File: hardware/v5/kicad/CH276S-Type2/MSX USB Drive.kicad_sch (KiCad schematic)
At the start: 11 parts, among them J1 AVR-JTAG-10, J2 Conn_02x08_Odd_Even, SW1 SK12D07VG4, U2 EPM7064STC44-7, U3 M29F400M

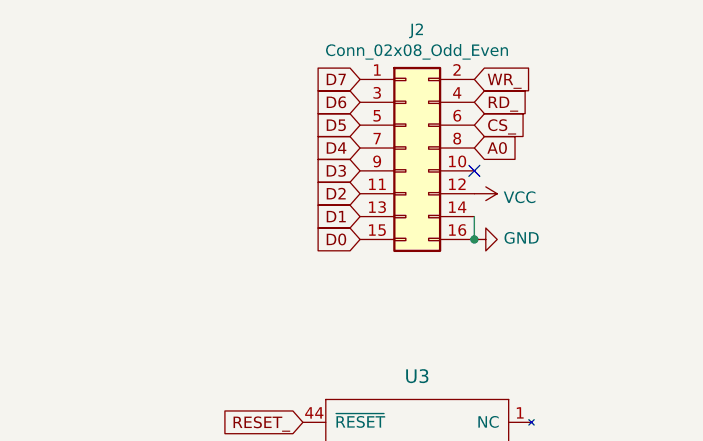
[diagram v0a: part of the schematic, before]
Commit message: cpld code and adjustments for v5
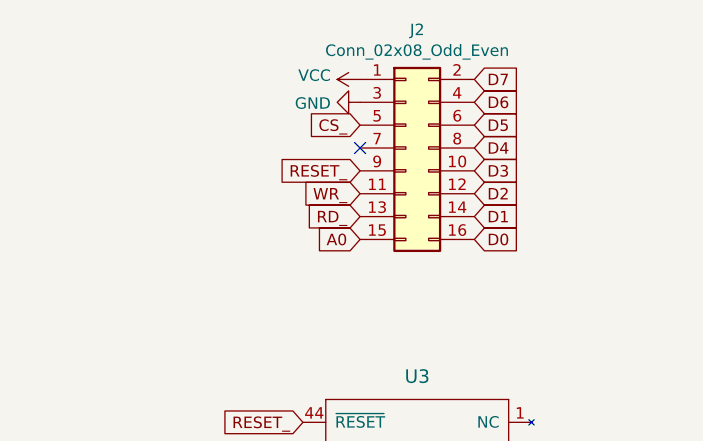
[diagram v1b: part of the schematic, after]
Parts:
- SW1: footprint SK12D07VG4 -> libraries:SK12D07VG4
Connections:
- net A0: now also J2.15 (Pin_15); no longer J2.8 (Pin_8)
- net CS_: now also J2.5 (Pin_5); no longer J2.6 (Pin_6)
- net D0: now also J2.16 (Pin_16); no longer J2.15 (Pin_15)
- net D1: now also J2.14 (Pin_14); no longer J2.13 (Pin_13)
- net D2: now also J2.12 (Pin_12); no longer J2.11 (Pin_11)
- net D3: now also J2.10 (Pin_10); no longer J2.9 (Pin_9)
- net D4: now also J2.8 (Pin_8); no longer J2.7 (Pin_7)
- net D5: now also J2.6 (Pin_6); no longer J2.5 (Pin_5)
- net D6: now also J2.4 (Pin_4); no longer J2.3 (Pin_3)
- net D7: now also J2.2 (Pin_2); no longer J2.1 (Pin_1)
- net GND: now also J2.3 (Pin_3); no longer J2.14 (Pin_14), J2.16 (Pin_16)
- net RD_: now also J2.13 (Pin_13); no longer J2.4 (Pin_4)
- net RESET_: now also J2.9 (Pin_9)
- net VCC: now also J2.1 (Pin_1); no longer J2.12 (Pin_12)
- net WR_: now also J2.11 (Pin_11); no longer J2.2 (Pin_2)
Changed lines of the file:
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@@
 	(title_block
 		(title "MSX-USB")
-		(date "2024-10-12")
+		(date "2024-11-18")
 		(rev "5.0")
 		(company "The Retro Hacker")
+		(comment 1 "Suitable for the CH376S Type 2")
 		(comment 2 "New PCB version, CPLD code by The Retro Hacker")
 		(comment 3 "Original project by S0urceror")
@@
 	)
 	(junction
-		(at 238.76 43.18)
-		(diameter 0)
-		(color 0 0 0 0)
-	)
-	(junction
 		(at 111.76 82.55)
 		(diameter 0)
@@
 	)
 	(no_connect
-		(at 238.76 35.56)
-	)
-	(no_connect
 		(at 245.11 91.44)
 	)
@@
 	)
 	(no_connect
+		(at 226.06 33.02)
+	)
+	(no_connect
 		(at 245.11 93.98)
 	)
@@
 	(wire
 		(pts
-			(xy 238.76 40.64) (xy 238.76 43.18)
-		)
-		(stroke
-			(width 0)
-			(type default)
-		)
-	)
-	(wire
-		(pts
 			(xy 260.35 133.35) (xy 259.08 133.35)
 		)
@@
 	(global_label "RD_"
 		(shape input)
-		(at 238.76 27.94 0)
+		(at 226.06 40.64 180)
 		(fields_autoplaced yes)
 		(effects
@@
 				(size 1.27 1.27)
 			)
-			(justify left)
+			(justify right)
 		)
 		(property "Intersheetrefs" "${INTERSHEET_REFS}"
-			(at 244.5986 27.94 0)
+			(at 220.2214 40.64 0)
 			(effects
 				(font
 					(size 1.27 1.27)
 				)
-				(justify left)
+				(justify right)
 				(hide yes)
 			)
@@
 	(global_label "A0"
 		(shape input)
-		(at 238.76 33.02 0)
+		(at 226.06 43.18 180)
 		(fields_autoplaced yes)
 		(effects
@@
 				(size 1.27 1.27)
 			)
-			(justify left)
+			(justify right)
 		)
 		(property "Intersheetrefs" "${INTERSHEET_REFS}"
-			(at 243.3891 33.02 0)
+			(at 221.4309 43.18 0)
 			(effects
 				(font
 					(size 1.27 1.27)
 				)
-				(justify left)
+				(justify right)
 				(hide yes)
 			)
@@
 	(global_label "D3"
 		(shape input)
-		(at 226.06 35.56 180)
+		(at 238.76 35.56 0)
 		(fields_autoplaced yes)
 		(effects
@@
 				(size 1.27 1.27)
 			)
-			(justify right)
+			(justify left)
 		)
 		(property "Intersheetrefs" "${INTERSHEET_REFS}"
-			(at 221.2495 35.56 0)
+			(at 243.5705 35.56 0)
 			(effects
 				(font
 					(size 1.27 1.27)
 				)
-				(justify right)
+				(justify left)
 				(hide yes)
 			)
@@
 	(global_label "D1"
 		(shape input)
-		(at 226.06 40.64 180)
+		(at 238.76 40.64 0)
 		(fields_autoplaced yes)
 		(effects
@@
 				(size 1.27 1.27)
 			)
-			(justify right)
+			(justify left)
 		)
 		(property "Intersheetrefs" "${INTERSHEET_REFS}"
-			(at 221.2495 40.64 0)
+			(at 243.5705 40.64 0)
 			(effects
 				(font
 					(size 1.27 1.27)
 				)
-				(justify right)
+				(justify left)
 				(hide yes)
 			)
@@
 	(global_label "WR_"
 		(shape input)
-		(at 238.76 25.4 0)
+		(at 226.06 38.1 180)
 		(fields_autoplaced yes)
 		(effects
@@
 				(size 1.27 1.27)
 			)
-			(justify left)
+			(justify right)
 		)
 		(property "Intersheetrefs" "${INTERSHEET_REFS}"
-			(at 244.78 25.4 0)
+			(at 220.04 38.1 0)
 			(effects
 				(font
 					(size 1.27 1.27)
 				)
-				(justify left)
+				(justify right)
 				(hide yes)
 			)
@@
 	(global_label "D2"
 		(shape input)
-		(at 226.06 38.1 180)
+		(at 238.76 38.1 0)
 		(fields_autoplaced yes)
 		(effects
@@
 				(size 1.27 1.27)
 			)
-			(justify right)
+			(justify left)
 		)
 		(property "Intersheetrefs" "${INTERSHEET_REFS}"
-			(at 221.2495 38.1 0)
+			(at 243.5705 38.1 0)
 			(effects
 				(font
 					(size 1.27 1.27)
 				)
-				(justify right)
+				(justify left)
 				(hide yes)
 			)
@@
 	(global_label "D5"
 		(shape input)
-		(at 226.06 30.48 180)
+		(at 238.76 30.48 0)
 		(fields_autoplaced yes)
 		(effects
@@
 				(size 1.27 1.27)
 			)
-			(justify right)
+			(justify left)
 		)
 		(property "Intersheetrefs" "${INTERSHEET_REFS}"
-			(at 221.2495 30.48 0)
+			(at 243.5705 30.48 0)
 			(effects
 				(font
 					(size 1.27 1.27)
 				)
-				(justify right)
+				(justify left)
 				(hide yes)
 			)
@@
 	(global_label "D6"
 		(shape input)
-		(at 226.06 27.94 180)
+		(at 238.76 27.94 0)
 		(fields_autoplaced yes)
 		(effects
@@
 				(size 1.27 1.27)
 			)
-			(justify right)
+			(justify left)
 		)
 		(property "Intersheetrefs" "${INTERSHEET_REFS}"
-			(at 221.2495 27.94 0)
+			(at 243.5705 27.94 0)
 			(effects
 				(font
 					(size 1.27 1.27)
 				)
-				(justify right)
+				(justify left)
 				(hide yes)
 			)
@@
 	(global_label "D7"
 		(shape input)
-		(at 226.06 25.4 180)
+		(at 238.76 25.4 0)
 		(fields_autoplaced yes)
 		(effects
@@
 				(size 1.27 1.27)
 			)
-			(justify right)
+			(justify left)
 		)
 		(property "Intersheetrefs" "${INTERSHEET_REFS}"
-			(at 221.2495 25.4 0)
+			(at 243.5705 25.4 0)
 			(effects
 				(font
 					(size 1.27 1.27)
 				)
-				(justify right)
+				(justify left)
 				(hide yes)
 			)
@@
 		)
 	)
+	(global_label "RESET_"
+		(shape input)
+		(at 226.06 35.56 180)
+		(fields_autoplaced yes)
+		(effects
+			(font
+				(size 1.27 1.27)
+			)
+			(justify right)
+		)
+		(property "Intersheetrefs" "${INTERSHEET_REFS}"
+			(at 217.0163 35.56 0)
+			(effects
+				(font
+					(size 1.27 1.27)
+				)
+				(justify right)
+				(hide yes)
+			)
+		)
+	)
 	(global_label "D0"
 		(shape input)
@@
 	(global_label "D4"
 		(shape input)
-		(at 226.06 33.02 180)
+		(at 238.76 33.02 0)
 		(fields_autoplaced yes)
 		(effects
@@
 				(size 1.27 1.27)
 			)
-			(justify right)
+			(justify left)
 		)
 		(property "Intersheetrefs" "${INTERSHEET_REFS}"
-			(at 221.2495 33.02 0)
+			(at 243.5705 33.02 0)
 			(effects
 				(font
 					(size 1.27 1.27)
 				)
-				(justify right)
+				(justify left)
 				(hide yes)
 			)
@@
 	(global_label "CS_"
 		(shape input)
-		(at 238.76 30.48 0)
+		(at 226.06 30.48 180)
 		(fields_autoplaced yes)
 		(effects
@@
 				(size 1.27 1.27)
 			)
-			(justify left)
+			(justify right)
 		)
 		(property "Intersheetrefs" "${INTERSHEET_REFS}"
-			(at 244.5381 30.48 0)
+			(at 220.2819 30.48 0)
 			(effects
 				(font
 					(size 1.27 1.27)
 				)
-				(justify left)
+				(justify right)
 				(hide yes)
 			)
@@
 	(global_label "D0"
 		(shape input)
-		(at 226.06 43.18 180)
+		(at 238.76 43.18 0)
 		(fields_autoplaced yes)
 		(effects
@@
 				(size 1.27 1.27)
 			)
-			(justify right)
+			(justify left)
 		)
 		(property "Intersheetrefs" "${INTERSHEET_REFS}"
-			(at 221.2495 43.18 0)
+			(at 243.5705 43.18 0)
 			(effects
 				(font
 					(size 1.27 1.27)
 				)
-				(justify right)
+				(justify left)
 				(hide yes)
 			)
@@
 	(symbol
 		(lib_id "power:GND")
-		(at 238.76 43.18 90)
+		(at 226.06 27.94 270)
 		(unit 1)
 		(exclude_from_sim no)
@@
 		(dnp no)
 		(property "Reference" "#PWR011"
-			(at 245.11 43.18 0)
+			(at 219.71 27.94 0)
 			(effects
 				(font
@@
 		)
 		(property "Value" "GND"
-			(at 242.0112 43.053 90)
+			(at 222.8088 28.067 90)
 			(effects
 				(font
@@
 		)
 		(property "Footprint" ""
-			(at 238.76 43.18 0)
+			(at 226.06 27.94 0)
 			(effects
 				(font
@@
 		)
 		(property "Datasheet" ""
-			(at 238.76 43.18 0)
+			(at 226.06 27.94 0)
 			(effects
 				(font
@@
 		)
 		(property "Description" ""
-			(at 238.76 43.18 0)
+			(at 226.06 27.94 0)
 			(effects
 				(font
@@
 	(symbol
 		(lib_id "power:VCC")
-		(at 238.76 38.1 270)
+		(at 226.06 25.4 90)
 		(unit 1)
 		(exclude_from_sim no)
@@
 		(dnp no)
 		(property "Reference" "#PWR010"
-			(at 234.95 38.1 0)
+			(at 229.87 25.4 0)
 			(effects
 				(font
@@
 		)
 		(property "Value" "VCC"
-			(at 242.0112 38.5318 90)
+			(at 222.8088 24.9682 90)
 			(effects
 				(font
@@
 		)
 		(property "Footprint" ""
-			(at 238.76 38.1 0)
+			(at 226.06 25.4 0)
 			(effects
 				(font
@@
 		)
 		(property "Datasheet" ""
-			(at 238.76 38.1 0)
+			(at 226.06 25.4 0)
 			(effects
 				(font
@@
 		)
 		(property "Description" ""
-			(at 238.76 38.1 0)
+			(at 226.06 25.4 0)
 			(effects
 				(font
@@
 			)
 		)
-		(property "Footprint" "SK12D07VG4"
+		(property "Footprint" "libraries:SK12D07VG4"
 			(at 106.68 168.91 0)
 			(effects

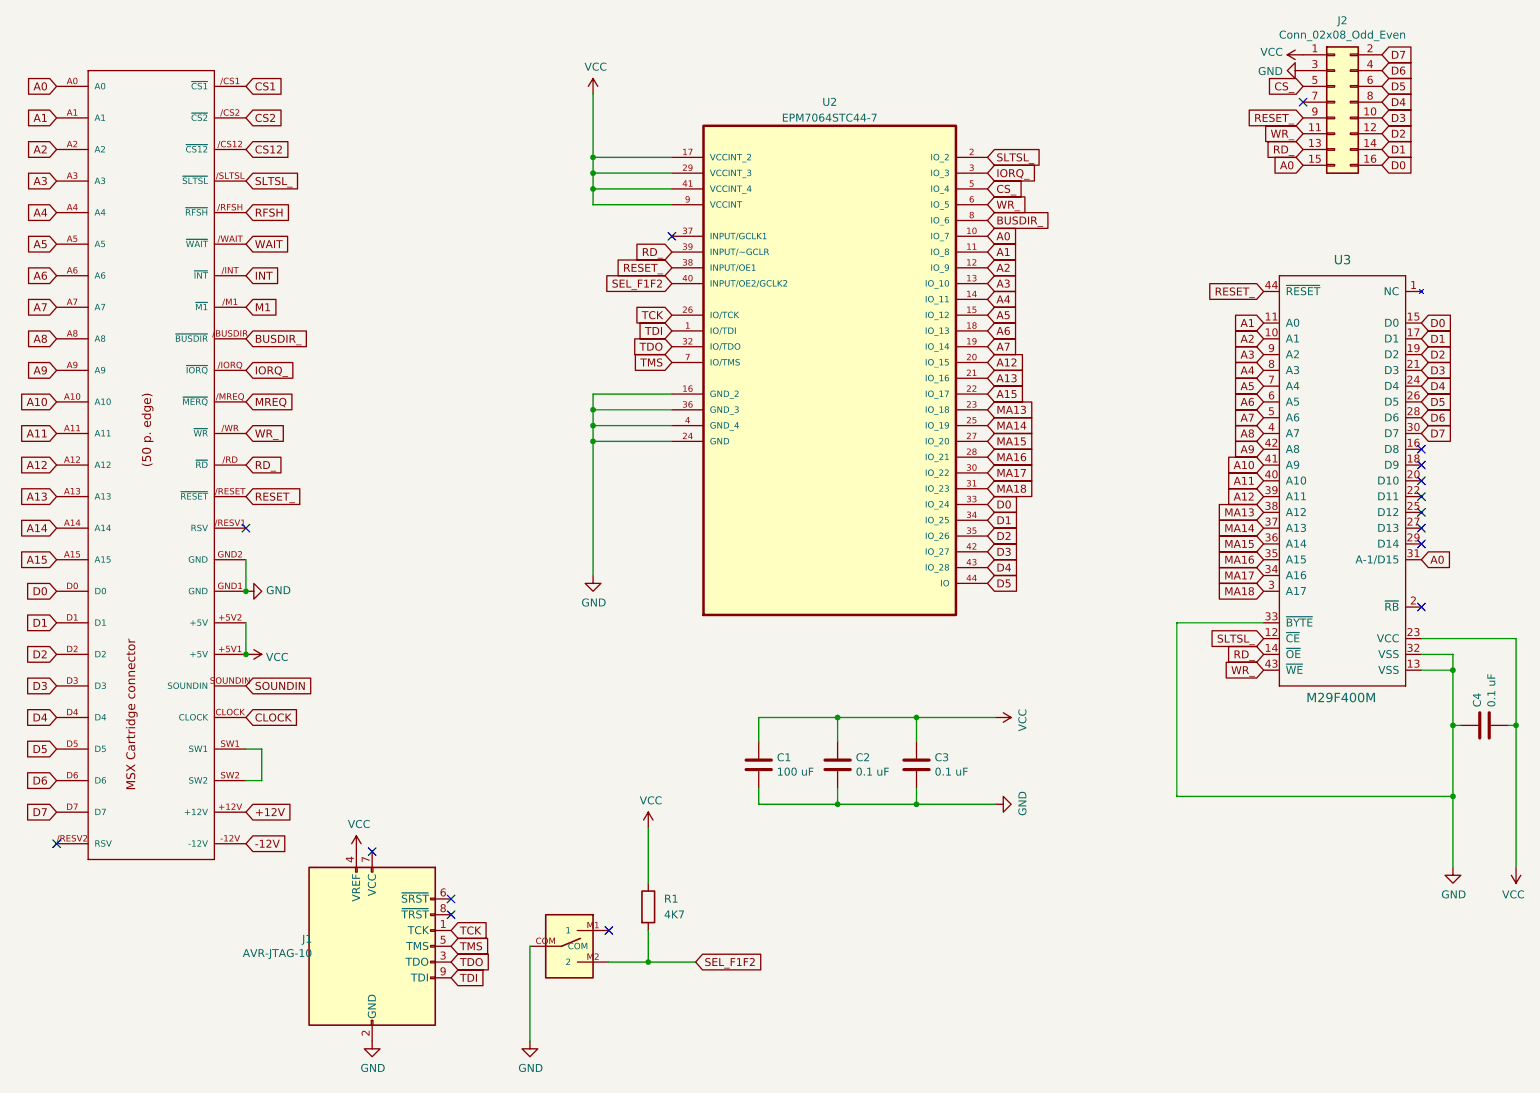
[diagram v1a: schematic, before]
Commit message: PCB adjustments for v5
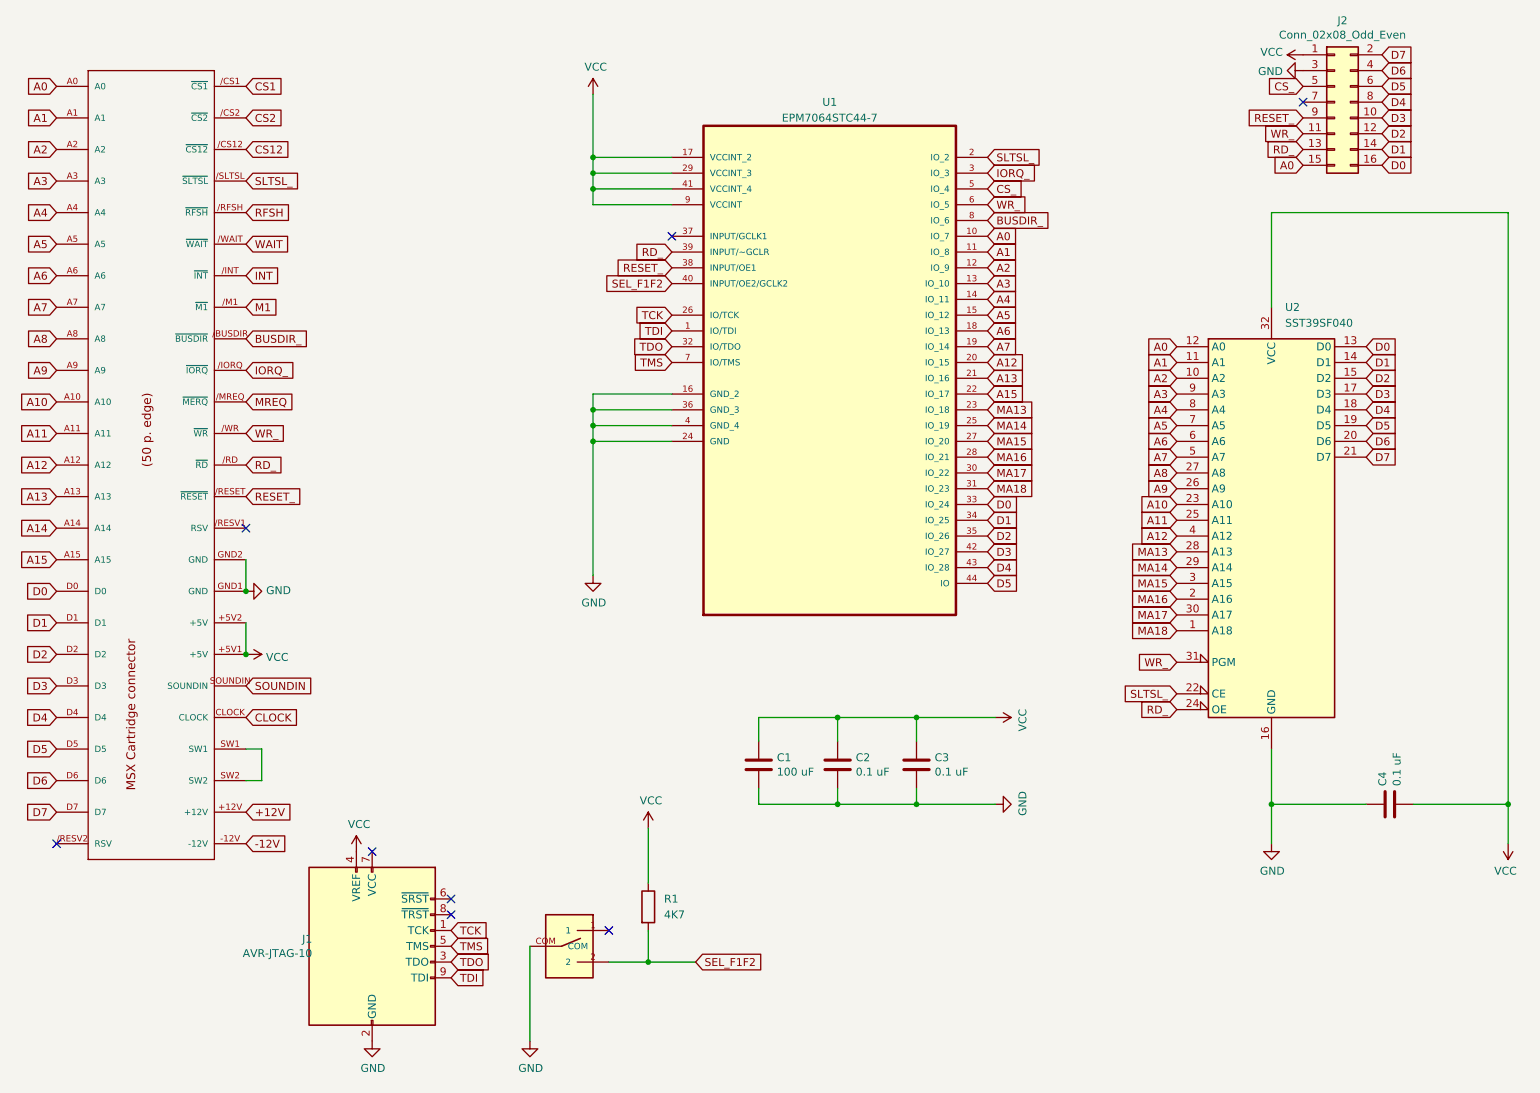
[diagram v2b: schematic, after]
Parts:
- removed U3: M29F400M, libraries:SO44, symbol m29f400m:M29F400M
- added U2: SST39SF040, Package_LCC:PLCC-32_THT-Socket, symbol Memory_Flash:SST39SF040
- SW1: footprint libraries:SK12D07VG4 -> SK12D07VG4
- renumbered U2 to U1
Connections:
- net A0: now also U2.12 (A0)
- net A1: now also U2.11 (A1)
- net A10: now also U2.23 (A10)
- net A11: now also U2.25 (A11)
- net A12: now also U2.4 (A12)
- net A2: now also U2.10 (A2)
- net A3: now also U2.9 (A3)
- net A4: now also U2.8 (A4)
- net A5: now also U2.7 (A5)
- net A6: now also U2.6 (A6)
- net A7: now also U2.5 (A7)
- net A8: now also U2.27 (A8)
- net A9: now also U2.26 (A9)
- net D0: now also U2.13 (D0)
- net D1: now also U2.14 (D1)
- net D2: now also U2.15 (D2)
- net D3: now also U2.17 (D3)
- net D4: now also U2.18 (D4)
- net D5: now also U2.19 (D5)
- net D6: now also U2.20 (D6)
- net D7: now also U2.21 (D7)
- net GND: now also U2.16 (GND)
- net MA13: now also U2.28 (A13)
- net MA14: now also U2.29 (A14)
- net MA15: now also U2.3 (A15)
- net MA16: now also U2.2 (A16)
- net MA17: now also U2.30 (A17)
- net MA18: now also U2.1 (A18)
- net RD_: now also U2.24 (OE)
- net SEL_F1F2: now also SW1.2; no longer SW1.M2 (2)
- net SLTSL_: now also U2.22 (CE)
- net VCC: now also U2.32 (VCC)
- net WR_: now also U2.31 (PGM)
- no-connect marks 16 -> 8

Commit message: PCB fixes
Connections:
- net RESET_: no longer J2.9 (Pin_9)
- no-connect marks 8 -> 9
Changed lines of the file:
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@@
 	(title_block
 		(title "MSX-USB")
-		(date "2024-11-20")
-		(rev "5.0")
+		(date "2024-12-20")
+		(rev "5.1")
 		(company "The Retro Hacker")
 		(comment 1 "Suitable for the CH376S Type 2")
@@
 	)
 	(no_connect
+		(at 226.06 35.56)
+	)
+	(no_connect
 		(at 55.88 101.6)
 	)
@@
 				(hide yes)
 			)
-		)
-	)
-	(global_label "RESET_"
-		(shape input)
-		(at 226.06 35.56 180)
-		(fields_autoplaced yes)
-		(effects
-			(font
-				(size 1.27 1.27)
-			)
-			(justify right)
-		)
-		(property "Intersheetrefs" "${INTERSHEET_REFS}"
-			(at 217.0163 35.56 0)
-			(effects
-				(font
-					(size 1.27 1.27)
-				)
-				(justify right)
-				(hide yes)
-			)
